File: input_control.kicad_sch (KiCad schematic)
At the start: 1 part, among them U1 CD4051BM

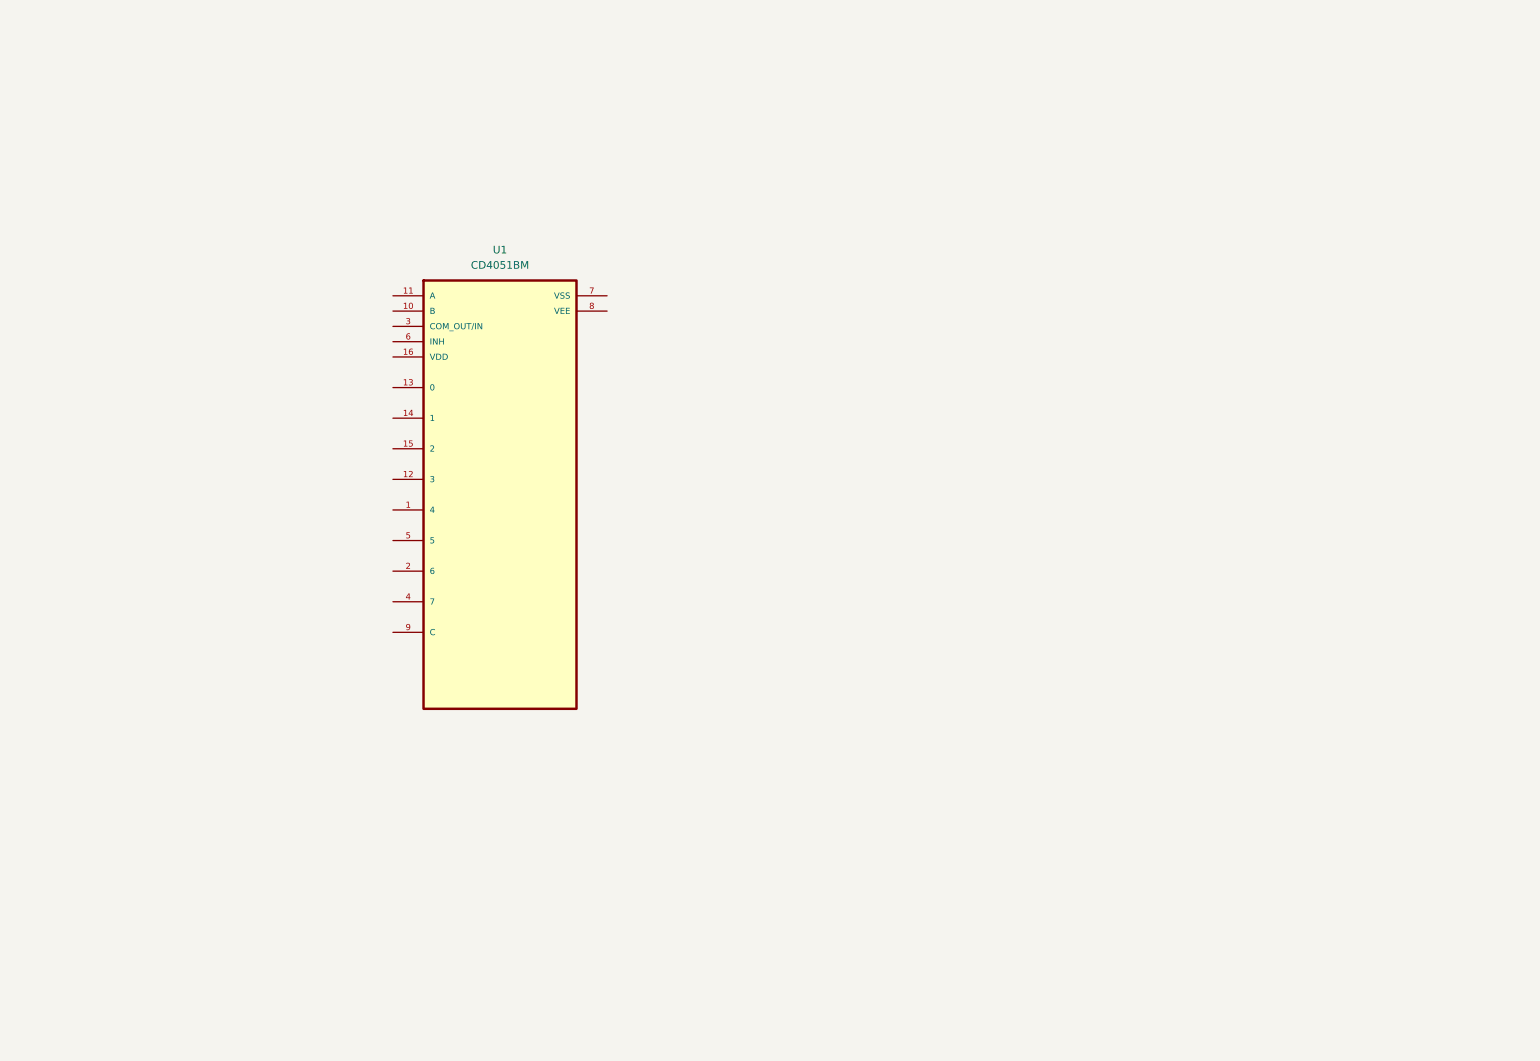
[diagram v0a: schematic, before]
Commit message: adde boot switch
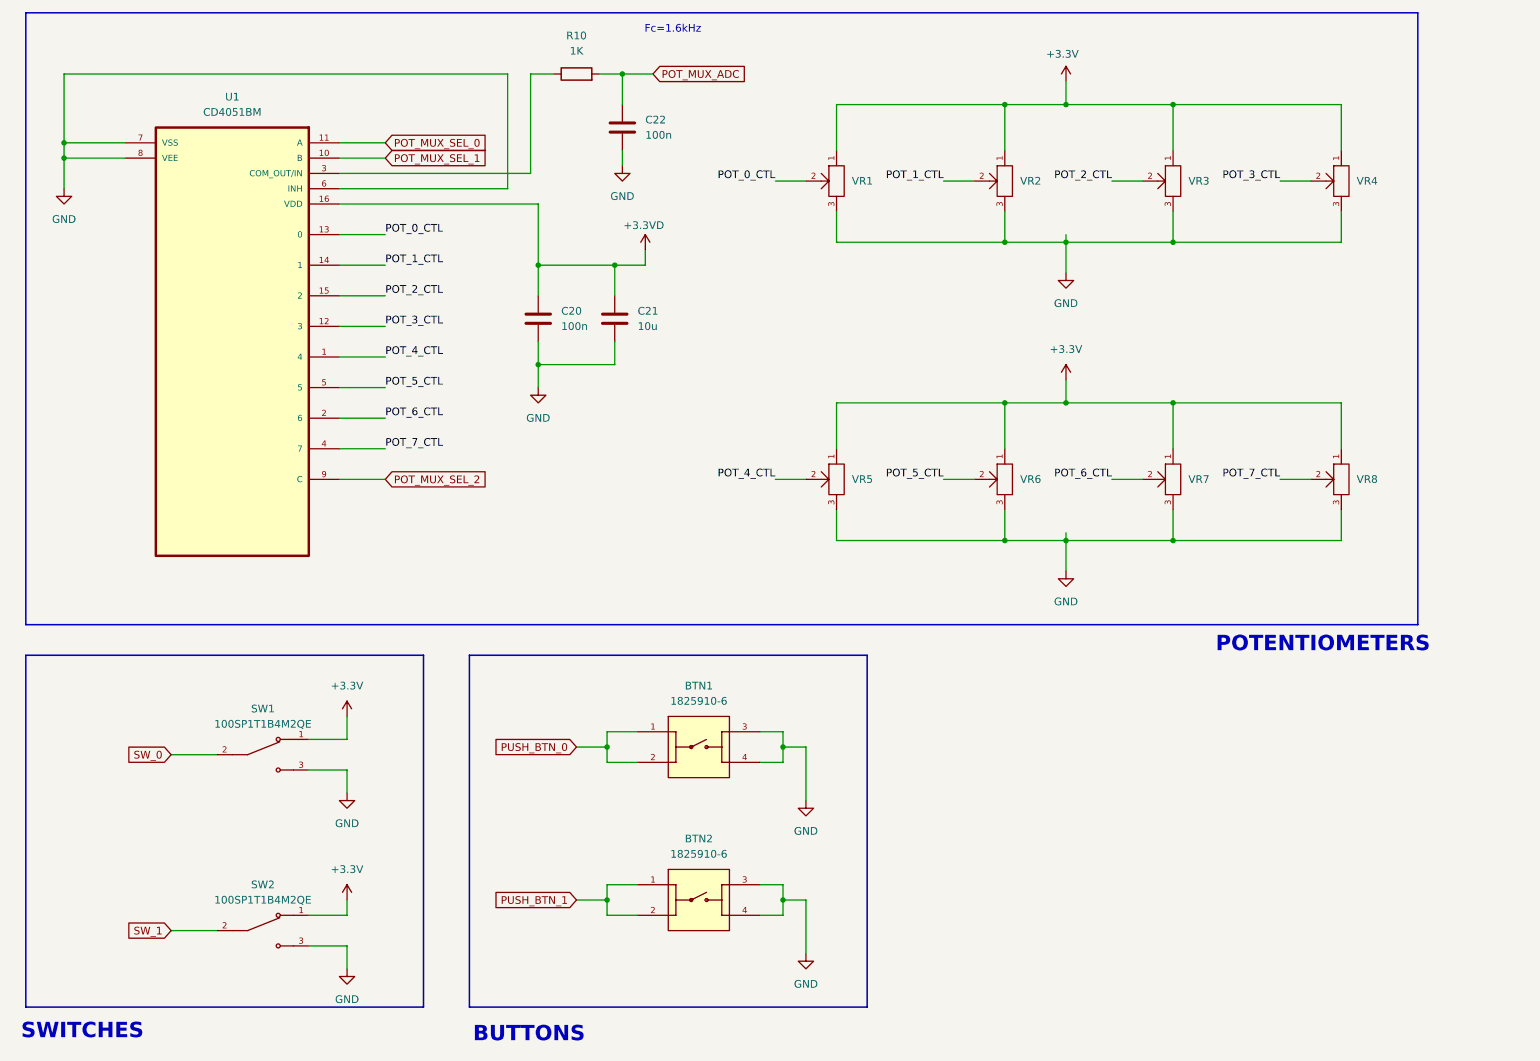
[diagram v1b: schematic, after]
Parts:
- added BTN1, BTN2: 1825910-6, Galerna:SW4_1825910-B_TEC, symbol Galerna:1825910-6
- added C20, C22: 100n, symbol Device:C
- added C21: 10u, symbol Device:C
- added R10: 1K, symbol Device:R
- added SW1, SW2: 100SP1T1B4M2QE, Galerna:SW_100SP1T1B4M2QE, symbol Galerna:100SP1T1B4M2QE
- added VR1, VR2, VR3, VR4, VR5, VR6, VR7, VR8: PTV09A-4225F-B104, Galerna:PTV09, symbol Galerna:PTV09A-4225F-B104
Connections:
- net POT_4_CTL: now reaches U1.1 (4)
- net POT_4_CTL: now also VR5.2
- net POT_MUX_SEL_1: now reaches U1.10 (B)
- net POT_MUX_SEL_0: now reaches U1.11 (A)
- net POT_3_CTL: now reaches U1.12 (3)
- net POT_3_CTL: now also VR4.2
- net POT_0_CTL: now reaches U1.13 (0)
- net POT_0_CTL: now also VR1.2
- net POT_1_CTL: now reaches U1.14 (1)
- net POT_1_CTL: now also VR2.2
- net POT_2_CTL: now reaches U1.15 (2)
- net POT_2_CTL: now also VR3.2
- net +3.3VD: now reaches U1.16 (VDD)
- net +3.3VD: now also C20.1, C21.1
- net POT_6_CTL: now reaches U1.2 (6)
- net POT_6_CTL: now also VR7.2
- net at U1.3 (COM_OUT/IN): now also R10.1
- net POT_7_CTL: now reaches U1.4 (7)
- net POT_7_CTL: now also VR8.2
- net POT_5_CTL: now reaches U1.5
- net POT_5_CTL: now also VR6.2
- net GND: now reaches U1.6 (INH)
- net GND: now also U1.7 (VSS), U1.8 (VEE), BTN1.3, BTN1.4, BTN2.3, BTN2.4, C20.2, C21.2, C22.2, SW1.3, SW2.3, VR1.3, VR2.3, VR3.3, VR4.3, VR5.3, VR6.3, VR7.3, VR8.3
- net POT_MUX_SEL_2: now reaches U1.9 (C)
- new net +3.3V: SW1.1, SW2.1, VR1.1, VR2.1, VR3.1, VR4.1, VR5.1, VR6.1, VR7.1, VR8.1
- new net POT_MUX_ADC: C22.1, R10.2
- new net PUSH_BTN_0: BTN1.1, BTN1.2
- new net PUSH_BTN_1: BTN2.1, BTN2.2
- new net SW_0: SW1.2
- new net SW_1: SW2.2
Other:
- note added: "BUTTONS"
- note added: "Fc=1.6kHz"
- note added: "POTENTIOMETERS"
- note added: "SWITCHES"
- moved on the sheet: U1

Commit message: MCU connected
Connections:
- net +3.3V renamed +3V3
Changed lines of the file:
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@@
 		(on_board yes)
 		(dnp no)
-		(fields_autoplaced yes)
 		(property "Reference" "#PWR029"
 			(at 76.2 135.89 0)
@@
 			)
 		)
-		(property "Value" "+3.3V"
-			(at 76.2 127 0)
-			(effects
-				(font
-					(size 1.27 1.27)
-				)
+		(property "Value" "+3V3"
+			(at 72.898 127.762 0)
+			(effects
+				(font
+					(size 1.27 1.27)
+				)
+				(justify left)
 			)
 		)
@@
 		(on_board yes)
 		(dnp no)
-		(fields_autoplaced yes)
 		(property "Reference" "#PWR030"
 			(at 76.2 166.37 0)
@@
 			)
 		)
-		(property "Value" "+3.3V"
-			(at 76.2 157.48 0)
-			(effects
-				(font
-					(size 1.27 1.27)
-				)
+		(property "Value" "+3V3"
+			(at 72.898 158.242 0)
+			(effects
+				(font
+					(size 1.27 1.27)
+				)
+				(justify left)
 			)
 		)
@@
 			)
 		)
-		(property "Value" "+3.3V"
-			(at 195.58 71.12 0)
-			(effects
-				(font
-					(size 1.27 1.27)
-				)
+		(property "Value" "+3V3"
+			(at 198.12 74.9299 0)
+			(effects
+				(font
+					(size 1.27 1.27)
+				)
+				(justify left)
 			)
 		)
@@
 			)
 		)
-		(property "Value" "+3.3V"
+		(property "Value" "+3V3"
 			(at 192.278 22.098 0)
 			(effects

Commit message: adding anotations
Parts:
- renumbered U1 to U8
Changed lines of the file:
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@@
 		(dnp no)
 		(fields_autoplaced yes)
-		(property "Reference" "#PWR?"
+		(property "Reference" "#PWR0123"
 			(at 195.58 64.77 0)
 			(effects
@@
 			(project "GalernaDsp"
 				(path "/a77f8f1b-3e6d-40f9-a36e-54a20299e9bc/9ff4b341-54b0-41b8-b594-0e1d528851b1"
-					(reference "#PWR?")
+					(reference "#PWR0123")
 					(unit 1)
 				)
@@
 		(on_board yes)
 		(dnp no)
-		(property "Reference" "#PWR?"
+		(property "Reference" "#PWR0122"
 			(at 195.58 30.48 0)
 			(effects
@@
 			(project "GalernaDsp"
 				(path "/a77f8f1b-3e6d-40f9-a36e-54a20299e9bc/9ff4b341-54b0-41b8-b594-0e1d528851b1"
-					(reference "#PWR?")
+					(reference "#PWR0122")
 					(unit 1)
 				)
@@
 		(on_board yes)
 		(dnp no)
-		(property "Reference" "U?"
+		(property "Reference" "U8"
 			(at 57.15 29.21 0)
 			(effects
@@
 			(project "GalernaDsp"
 				(path "/a77f8f1b-3e6d-40f9-a36e-54a20299e9bc/9ff4b341-54b0-41b8-b594-0e1d528851b1"
-					(reference "U?")
+					(reference "U8")
 					(unit 1)
 				)

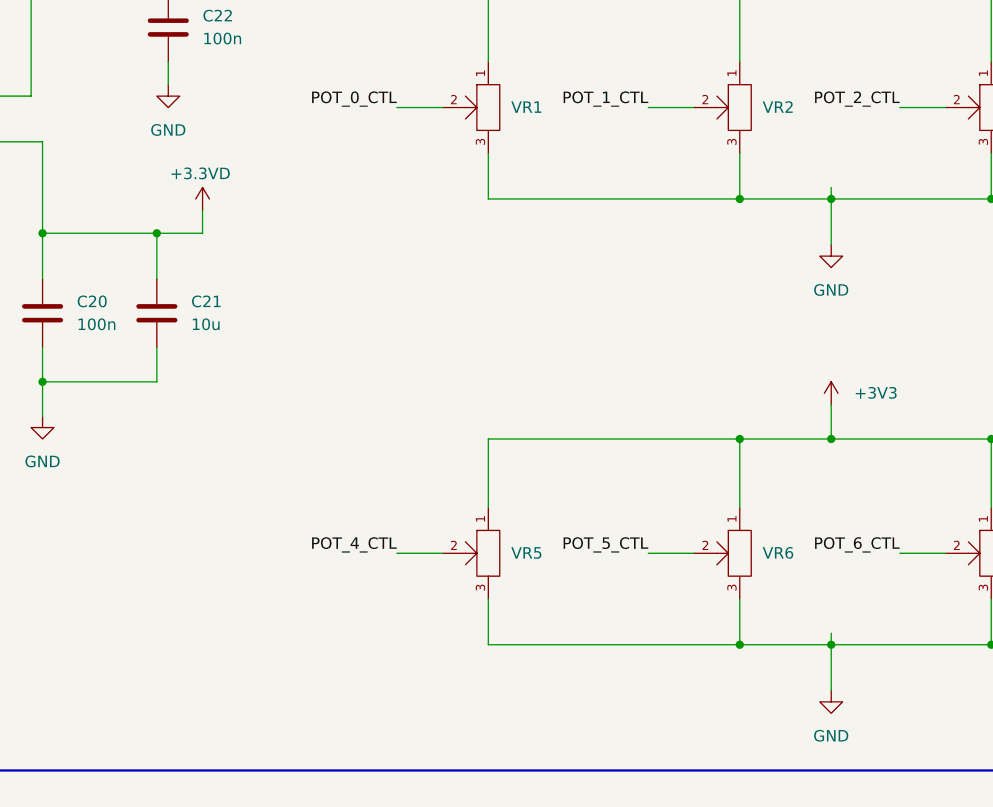
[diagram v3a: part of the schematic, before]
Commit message: ERC fixed
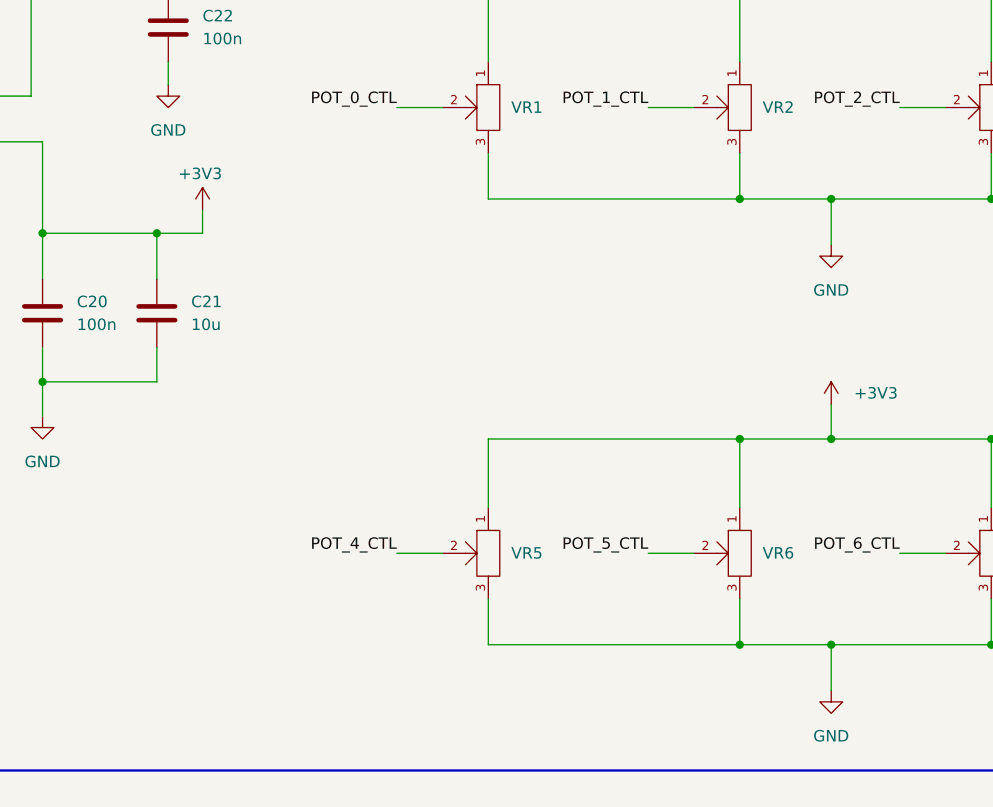
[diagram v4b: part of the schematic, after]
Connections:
- net +3.3VD is gone; now on net +3V3: C20.1, C21.1, U8.16 (VDD)
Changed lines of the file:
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@@
-	(wire
-		(pts
-			(xy 195.58 101.6) (xy 195.58 102.87)
-		)
-		(stroke
-			(width 0)
-			(type default)
-		)
-	)
 	(wire
 		(pts
@@
 		(pts
 			(xy 157.48 80.01) (xy 185.42 80.01)
-		)
-		(stroke
-			(width 0)
-			(type default)
-		)
-	)
-	(wire
-		(pts
-			(xy 195.58 52.07) (xy 195.58 53.34)
 		)
 		(stroke
@@
 			)
 		)
-		(property "Value" "+3.3VD"
+		(property "Value" "+3V3"
 			(at 125.476 50.546 0)
 			(effects

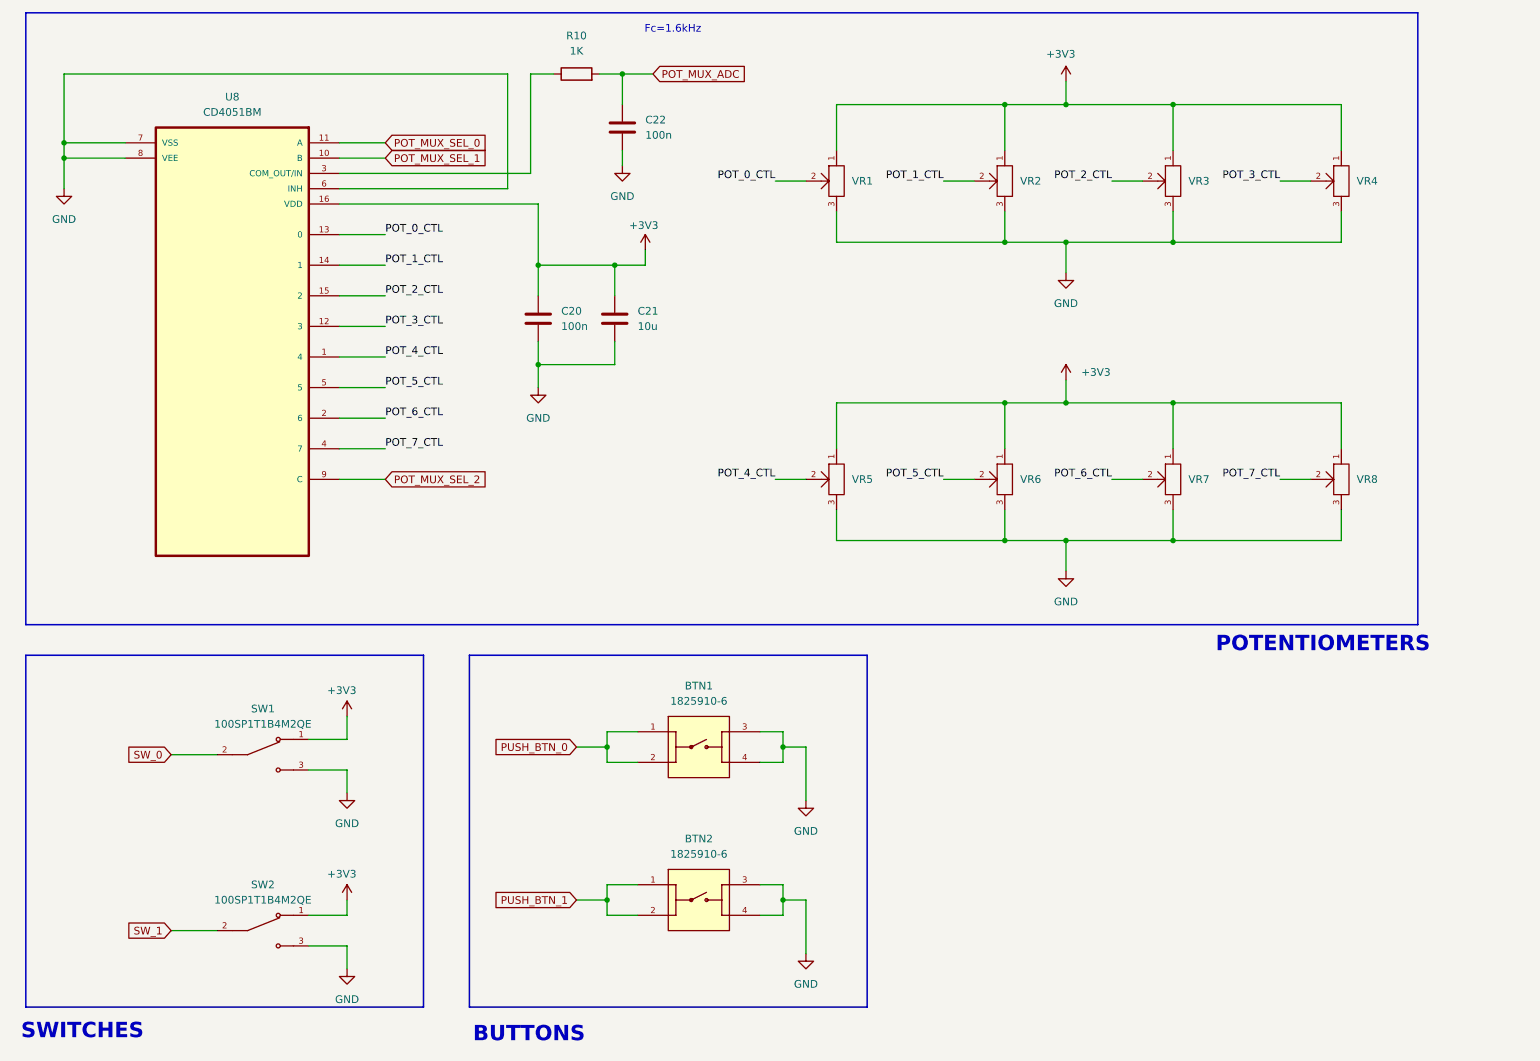
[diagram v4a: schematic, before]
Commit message: footprints updated
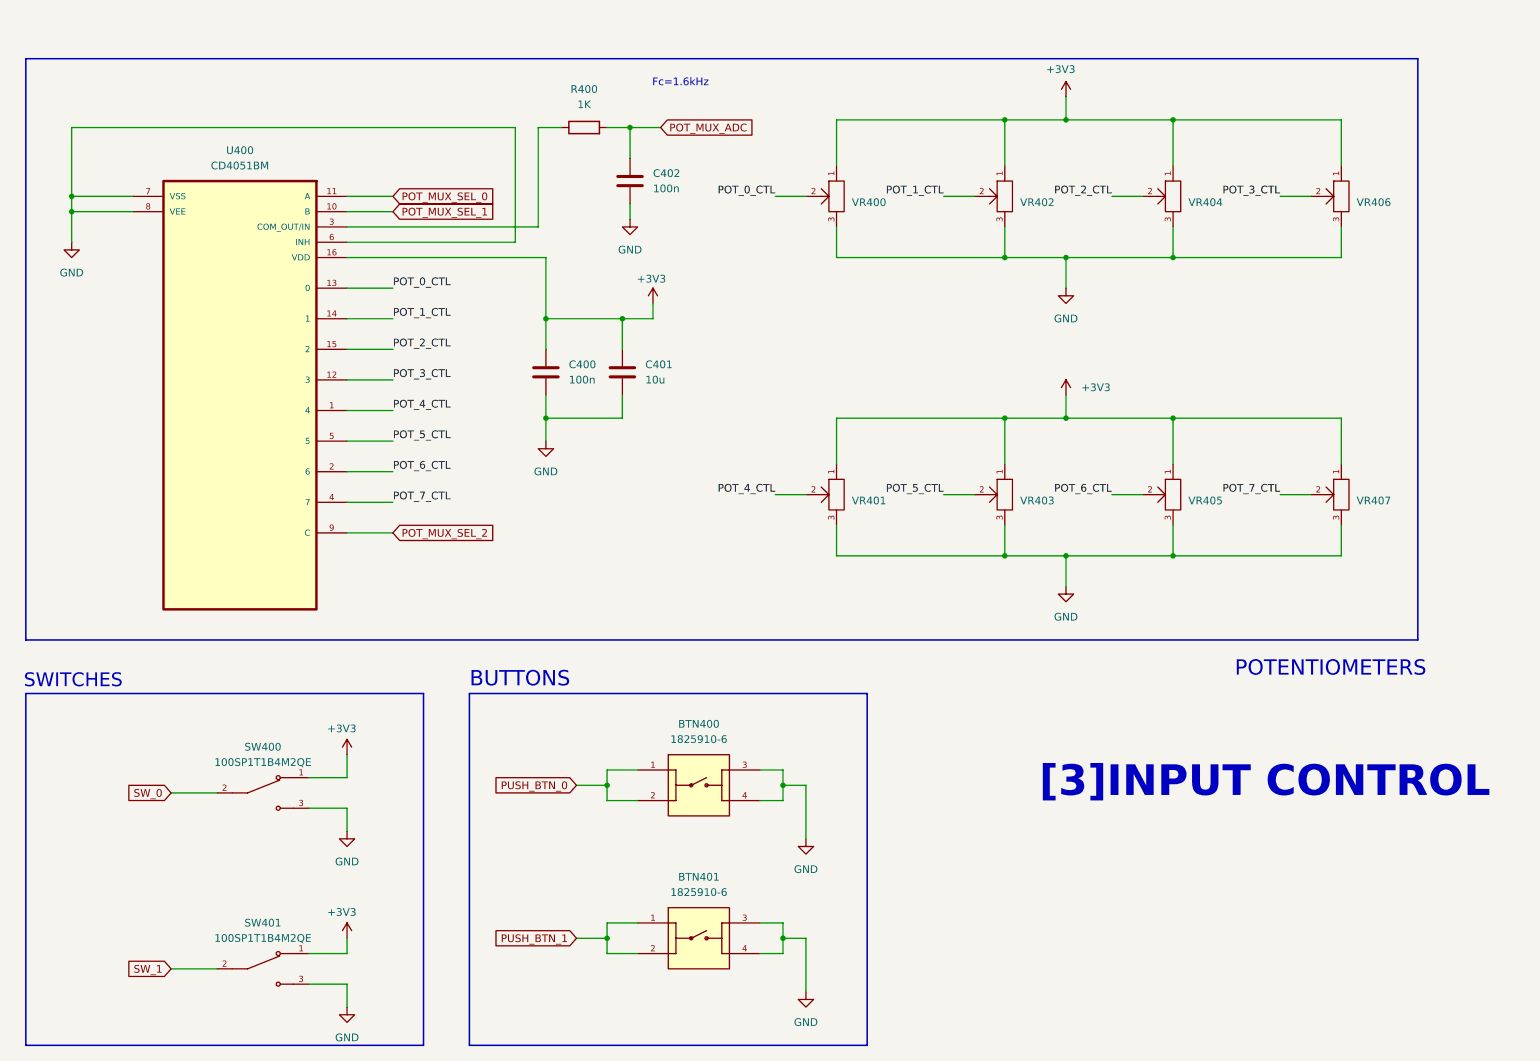
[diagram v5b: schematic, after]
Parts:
- C400: renamed from C20; footprint (none) -> Capacitor_SMD:C_0402_1005Metric
- C401: renamed from C21; footprint (none) -> Capacitor_SMD:C_0603_1608Metric
- C402: renamed from C22; footprint (none) -> Capacitor_SMD:C_0402_1005Metric
- R400: renamed from R10; footprint (none) -> Resistor_SMD:R_0402_1005Metric
- renumbered BTN1 to BTN400, BTN2 to BTN401, SW1 to SW400, SW2 to SW401, U8 to U400, VR1 to VR400, VR5 to VR401, VR2 to VR402, VR6 to VR403, VR3 to VR404, VR7 to VR405, VR4 to VR406, VR8 to VR407
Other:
- note added: "[3]INPUT CONTROL"
- moved on the sheet: BTN400, BTN401, C400, C401, C402, R400, SW400, SW401, U400, VR400, VR401, VR402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
